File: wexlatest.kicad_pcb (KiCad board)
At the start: 2 copper layers, 51 parts, among them J1 Screw_Terminal_01x02, J2 Conn_02x10_Odd_Even, J3 DB25_Female, J4 PROG, J5 Conn_02x06_Odd_Even, SW1 SW_Push, SW10 SW_DIP_x06, SW2 SW_Push, SW3 SW_Push, SW4 SW_Push, SW5 SW_DIP_x01, SW6 SW_Push, SW7 SW_Push, SW8 SW_Push, SW9 SW_Push

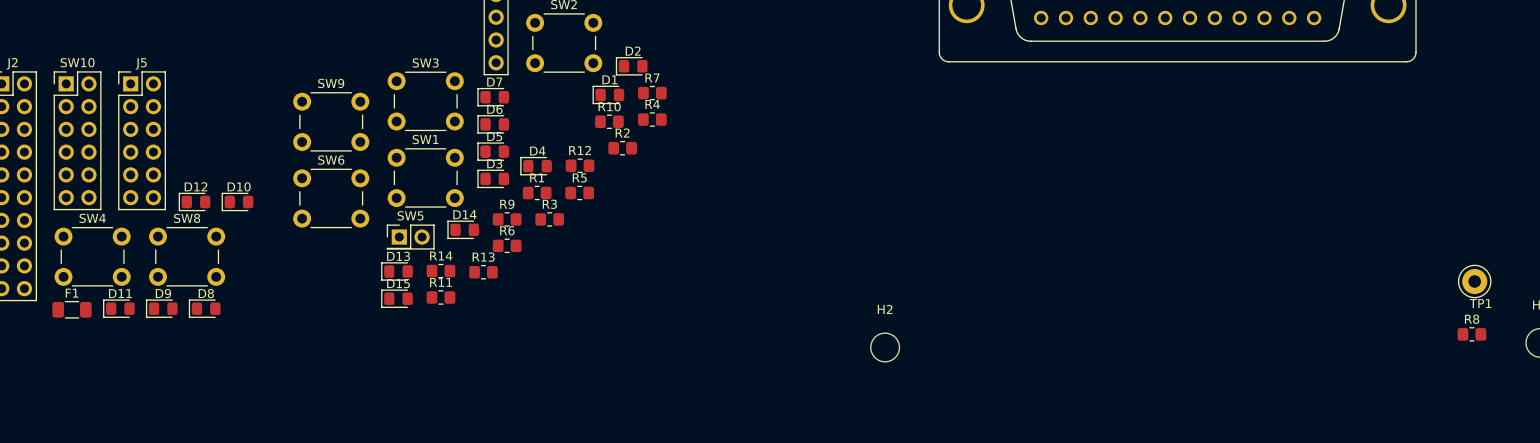
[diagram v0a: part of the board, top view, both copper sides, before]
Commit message: Add KK254 connector.
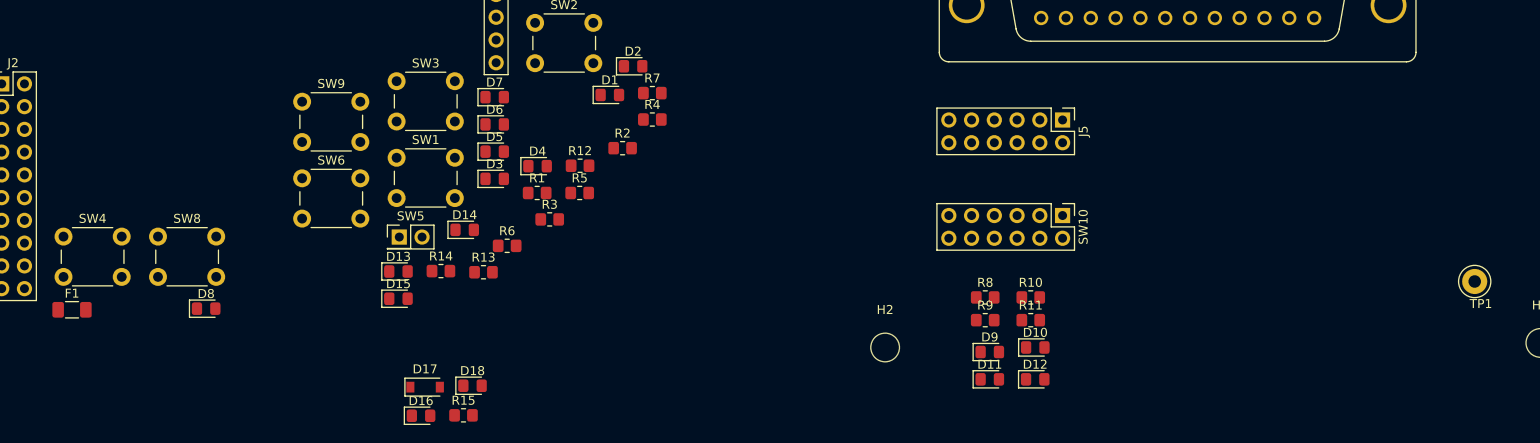
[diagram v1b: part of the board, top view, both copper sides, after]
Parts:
- added D16: GR, LED_SMD:LED_0805_2012Metric_Pad1.15x1.40mm_HandSolder, F.Cu at (73.7, 104.6)
- added D17: 1N4007, Diode_SMD:D_SOD-123, F.Cu at (74.1, 101.5)
- added D18: 1N4148, Diode_SMD:D_0805_2012Metric_Pad1.15x1.40mm_HandSolder, F.Cu at (79.4, 101.3)
- added R15: 1k, Resistor_SMD:R_0805_2012Metric_Pad1.20x1.40mm_HandSolder, F.Cu at (78.4, 104.6)
- moved SW10 112.2 mm to (145.3, 82.3), turned to 270 degrees
- moved J5 104.1 mm to (145.3, 71.6), turned to 270 degrees
- moved D11 97.4 mm to (137.2, 100.6)
- moved D12 95.8 mm to (142.2, 100.6)
- moved D9 92.4 mm to (137.2, 97.5)
- moved D10 90.4 mm to (142.2, 97.0)
- moved R11 65.9 mm to (141.7, 94.0)
- moved R9 54.5 mm to (136.7, 94.0)
- moved R8 54.5 mm to (136.7, 91.4)
- moved R10 51.0 mm to (141.7, 91.4)
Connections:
- D2 pad 1: +12V -> Net-(D17-Pad2)
- D2 pad 2: Net-(D2-Pad2) -> Net-(D18-Pad1)
- F1 pad 2: +12V -> Net-(D17-Pad2)
- R5 pad 1: Net-(D2-Pad2) -> Net-(D18-Pad2)

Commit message: Add initial PCB layout.
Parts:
- added J6: Conn_01x04, Connector_Molex:Molex_KK-254_AE-6410-04A_1x04_P2.54mm_Vertical, F.Cu at (194.1, 76.2)
- R10, R11, R8, R9: moved to B.Cu
- moved F1 185.5 mm to (219.4, 109.2)
- moved J2 156.8 mm to (183.4, 77.2), turned to 270 degrees
- moved D17 151.9 mm to (226.1, 102.1)
- moved D18 140.1 mm to (219.5, 105.7)
- moved SW4 138.0 mm to (169.2, 111.3), turned to 90 degrees
- moved D1 137.4 mm to (227.1, 105.7)
- moved D2 136.4 mm to (226.6, 109.2)
- moved R5 133.4 mm to (223.5, 98.0)
- moved D8 127.9 mm to (171.2, 132.6)
- moved R4 123.1 mm to (218.9, 101.1)
- moved SW5 116.8 mm to (183.9, 115.6), turned to 270 degrees
- moved J4 112.8 mm to (194.8, 54.9)
- moved SW7 112.6 mm to (169.2, 128.5), turned to 90 degrees
- moved SW6 111.6 mm to (160.0, 128.5), turned to 90 degrees
- moved SW9 108.0 mm to (150.9, 128.5), turned to 90 degrees
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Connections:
- SW10 pad 1: Net-(D12-Pad1) -> RELAL
- SW10 pad 10: RELAR -> GND
- SW10 pad 11: RELBL -> RELBR
- SW10 pad 12: RELBR -> Net-(D12-Pad1)
- SW10 pad 2: Net-(D11-Pad1) -> Net-(D9-Pad1)
- SW10 pad 3: Net-(D10-Pad1) -> RELAM
- SW10 pad 4: Net-(D9-Pad1) -> GND
- SW10 pad 5: GND -> RELAR
- SW10 pad 6: GND -> Net-(D10-Pad1)
- SW10 pad 7: RELAM -> RELBL
- SW10 pad 8: RELBM -> Net-(D11-Pad1)
- SW10 pad 9: RELAL -> RELBM

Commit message: PCB: add some wires
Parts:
- moved D2 111.5 mm to (118.1, 83.3), turned to 270 degrees
- moved D1 106.8 mm to (122.7, 83.3), turned to 90 degrees
- moved R5 105.6 mm to (118.1, 92.5), turned to 270 degrees
- moved D18 102.9 mm to (118.1, 87.9), turned to 270 degrees
- moved J1 100.6 mm to (123.0, 103.0), turned to 270 degrees
- moved D17 100.6 mm to (127.3, 83.3), turned to 270 degrees
- moved R4 96.7 mm to (122.7, 92.5), turned to 270 degrees
- moved F1 93.7 mm to (127.3, 92.5), turned to 90 degrees
- moved TP1 92.9 mm to (123.0, 120.0)
- moved J4 47.5 mm to (195.0, 102.4)
- moved H5 37.7 mm to (195.0, 134.0)
- moved H2 37.2 mm to (121.0, 134.0)
- moved D4 34.8 mm to (136.5, 112.4)
- moved R13 33.5 mm to (137.2, 101.0), turned to 0 degrees
- moved D14 33.2 mm to (137.2, 104.8), turned to 0 degrees
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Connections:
- J5 pad 1: RELAL -> RELBL
- J5 pad 10: RELBM -> RELAM
- J5 pad 11: RELBR -> RELAL
- J5 pad 12: RELBR -> RELAL
- J5 pad 2: RELAL -> RELBL
- J5 pad 3: RELAM -> RELBM
- J5 pad 4: RELAM -> RELBM
- J5 pad 5: RELAR -> RELBR
- J5 pad 6: RELAR -> RELBR
- J5 pad 7: RELBL -> RELAR
- J5 pad 8: RELBL -> RELAR
- J5 pad 9: RELBM -> RELAM
- SW10 pad 1: RELAL -> RELBL
- SW10 pad 11: RELBR -> RELAL
- SW10 pad 3: RELAM -> RELBM
- SW10 pad 5: RELAR -> RELBR
- SW10 pad 7: RELBL -> RELAR
- SW10 pad 9: RELBM -> RELAM
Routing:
- net +12V: track 0.00 -> 116.8 mm
- net +5V: track 0.00 -> 75.6 mm, vias 0 -> 2
- net RELAL: track 0.00 -> 66.5 mm
- net RELAM: track 0.00 -> 54.2 mm
- net IN-SLAVE|MCLR: track 0.00 -> 34.8 mm
- net IN-: track 0.00 -> 34.7 mm
- net IN+: track 0.00 -> 34.3 mm
- net RELAR: track 0.00 -> 33.3 mm
- net RELBL: track 0.00 -> 32.5 mm
- net RELBM: track 0.00 -> 31.2 mm
- net RELBR: track 0.00 -> 30.0 mm
- net OUT-: track 0.00 -> 24.8 mm
- net BTN-|PGD: track 0.00 -> 24.7 mm
- net BTN+|PGC: track 0.00 -> 24.7 mm
- net OUT+: track 0.00 -> 24.3 mm
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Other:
- board outline added: 86 x 100 mm
- board text added: "+12V"
- board text added: "+5V"
- board text added: "1"
- board text added: "13"
- board text added: "14"
- board text added: "25"
- board text added: "5V VALID"
- board text added: "BTN+"
- board text added: "BTN-"
- board text added: "GND"
- board text added: "IN+"
- board text added: "IN-"
- board text added: "L"
- board text added: "M"
- board text added: "OUT+"
- board text added: "OUT-"
- board text added: "POWER"
- board text added: "R"
- board text added: "RELA"
- board text added: "RELB"
- board text added: "SHORT"
- board text added: "SLAVE"

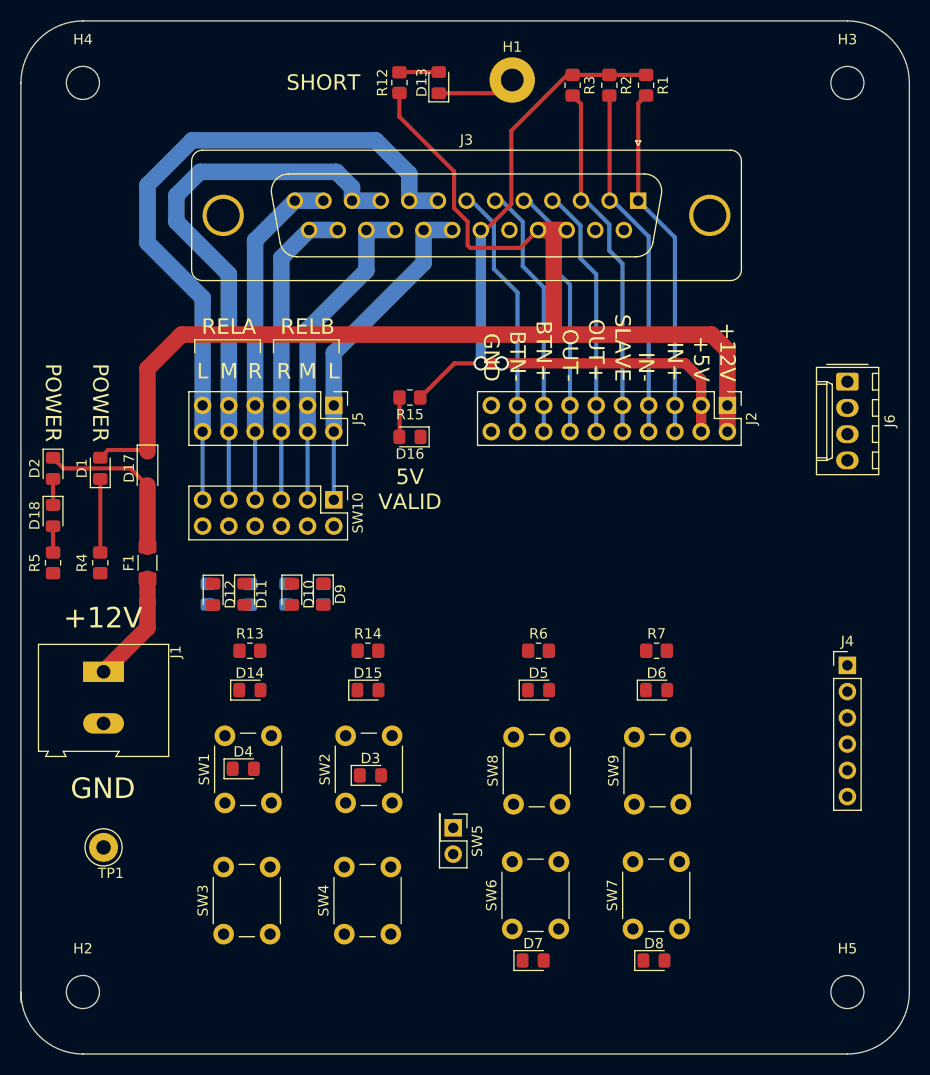
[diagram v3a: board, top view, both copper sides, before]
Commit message: PCB: trace all wires, first prototype.
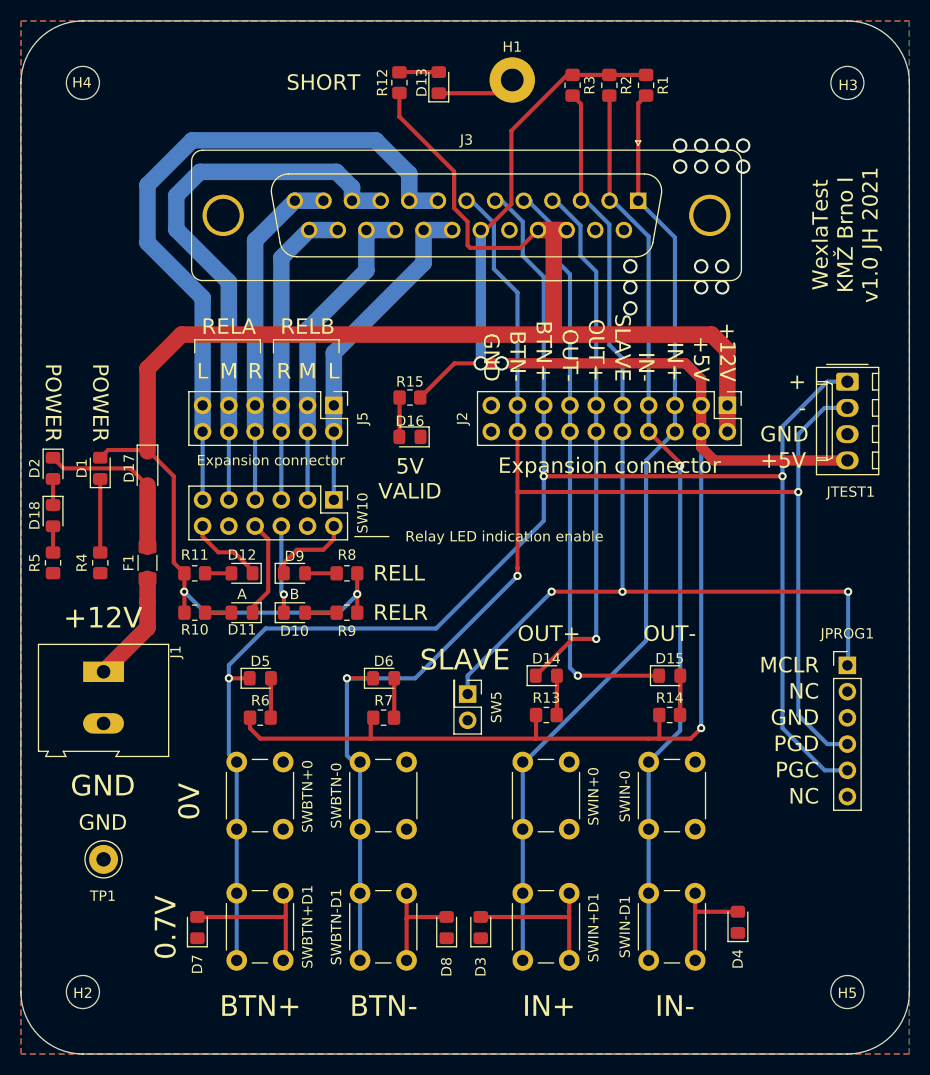
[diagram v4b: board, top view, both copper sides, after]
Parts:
- removed J6: Conn_01x04, Connector_Molex:Molex_KK-254_AE-6410-04A_1x04_P2.54mm_Vertical
- removed SW1, SW2, SW3, SW4, SW8, SW9: SW_Push, Button_Switch_THT:SW_PUSH_6mm
- added JTEST1: Conn_01x04, Connector_Molex:Molex_KK-254_AE-6410-04A_1x04_P2.54mm_Vertical, F.Cu at (195.0, 74.9)
- added SWBTN+0: SW_Push, Button_Switch_THT:SW_PUSH_6mm, F.Cu at (135.9, 118.2)
- added SWBTN-0: SW_Push, Button_Switch_THT:SW_PUSH_6mm, F.Cu at (147.8, 118.2)
- added SWIN+0: SW_Push, Button_Switch_THT:SW_PUSH_6mm, F.Cu at (163.6, 118.2)
- added SWIN+D1: SW_Push, Button_Switch_THT:SW_PUSH_6mm, F.Cu at (163.6, 130.9)
- added SWIN-0: SW_Push, Button_Switch_THT:SW_PUSH_6mm, F.Cu at (175.8, 118.2)
- added SWIN-D1: SW_Push, Button_Switch_THT:SW_PUSH_6mm, F.Cu at (175.8, 130.9)
- R10, R11, R8, R9: moved to F.Cu
- moved D4 50.1 mm to (184.4, 127.3), turned to 90 degrees
- moved D7 32.7 mm to (132.1, 127.8), turned to 90 degrees
- moved R14 29.9 mm to (177.8, 107.2)
- moved R13 29.4 mm to (165.9, 107.2)
- moved D15 29.2 mm to (177.8, 103.4)
- moved D14 28.7 mm to (165.9, 103.4)
- moved R6 27.7 mm to (138.2, 107.4)
- moved R7 27.2 mm to (150.1, 107.4)
- moved D5 26.9 mm to (138.2, 103.6)
- moved SWBTN+D1 26.8 mm to (135.9, 130.9)
- moved SWBTN-D1 26.6 mm to (147.8, 130.9)
- moved D6 26.4 mm to (150.1, 103.6)
- moved D8 20.3 mm to (156.2, 127.8), turned to 90 degrees
- moved D3 18.2 mm to (159.5, 127.8), turned to 90 degrees
- moved SW5 13.0 mm to (158.2, 105.2)
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- renumbered J4 to JPROG1, SW6 to SWBTN+D1, SW7 to SWBTN-D1
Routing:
- net BTN+|PGC: track 24.7 -> 169.8 mm, vias 0 -> 3
- net BTN-|PGD: track 24.7 -> 155.7 mm, vias 0 -> 3
- net +5V: track 75.6 -> 172.7 mm, vias 2 -> 3
- net IN-SLAVE|MCLR: track 34.8 -> 99.4 mm, vias 0 -> 3
- net IN+: track 34.3 -> 92.1 mm
- net IN-: track 34.7 -> 88.4 mm, vias 0 -> 1
- net +12V: track 116.8 -> 156.4 mm, vias 0 -> 2
- net OUT-: track 24.8 -> 56.3 mm, vias 0 -> 1
- net OUT+: track 24.3 -> 51.9 mm, vias 0 -> 1
- net Net-(D3-Pad2): track 0.00 -> 15.2 mm
- net Net-(D7-Pad2): track 0.00 -> 15.1 mm
- net Net-(D4-Pad2): track 0.00 -> 10.7 mm
- net Net-(D8-Pad2): track 0.00 -> 10.5 mm
- net Net-(D11-Pad1): track 0.00 -> 9.54 mm
- net Net-(D10-Pad1): track 0.00 -> 8.48 mm, vias 0 -> 1
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- added copper zone on B.Cu, net GND
- added copper zone on F.Cu, net GND
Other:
- outline, holes or cut-outs redrawn
- board text added: "+"
- board text added: "-"
- board text added: "0.7V"
- board text added: "0V"
- board text added: "A"
- board text added: "B"
- board text added: "Expansion connector"
- board text added: "MCLR"
- board text added: "NC"
- board text added: "PGC"
- board text added: "PGD"
- board text added: "RELL"
- board text added: "RELR"
- board text added: "Relay LED indication enable"
- board text added: "WexlaTest KMŽ Brno I v1.0 JH 2021"

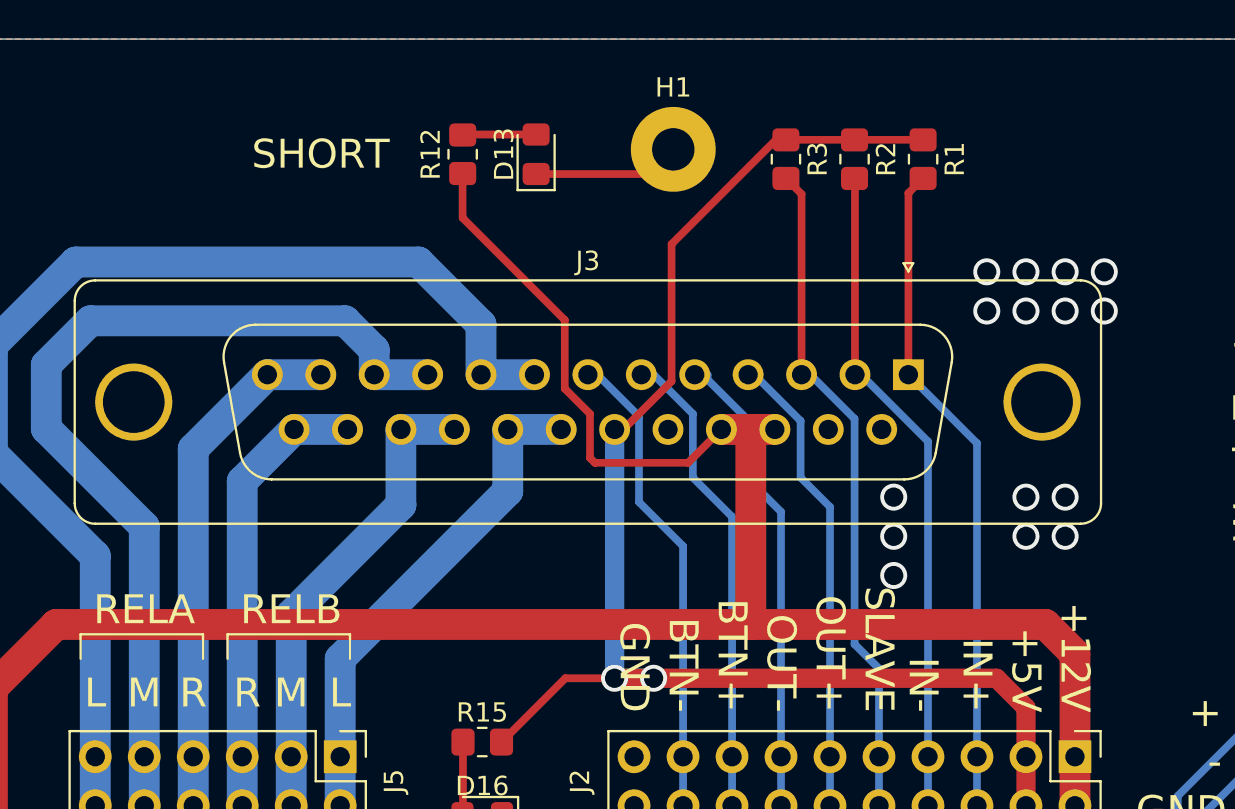
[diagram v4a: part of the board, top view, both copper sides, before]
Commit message: Add holes for mechanical test of turnout force.
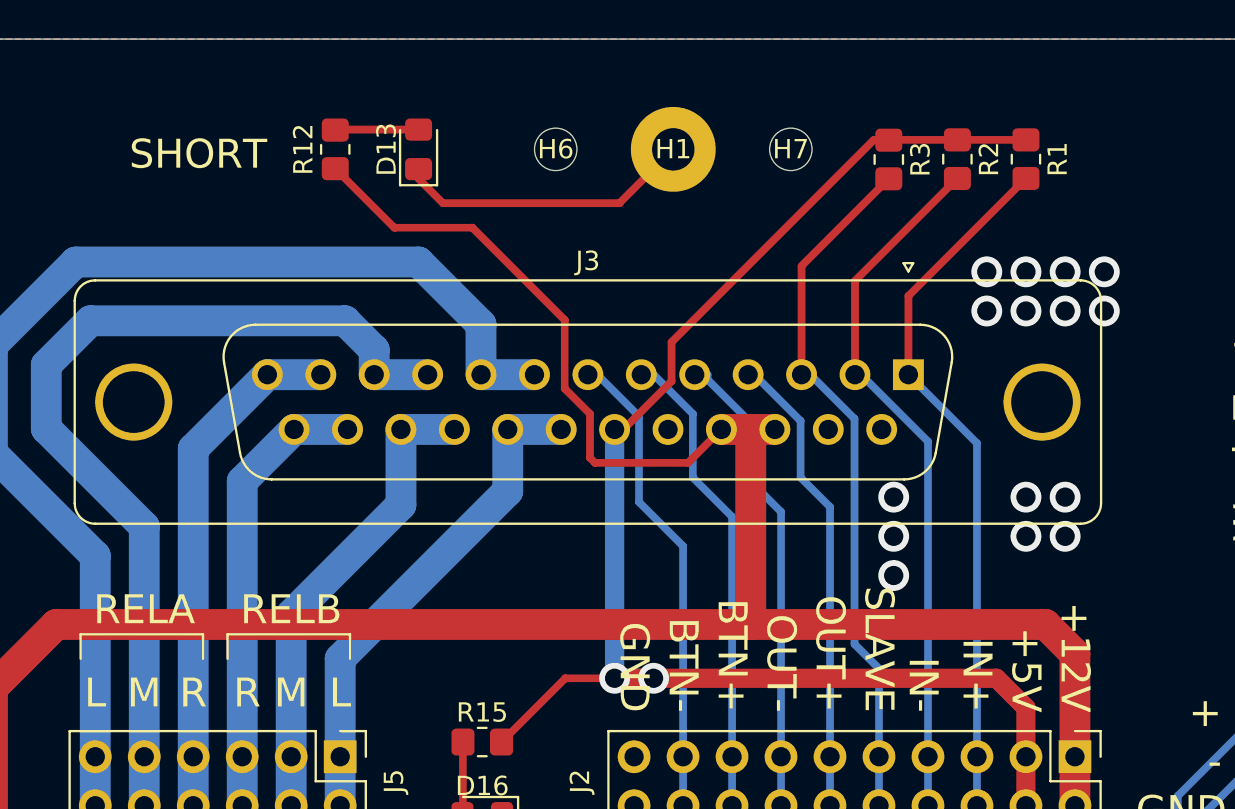
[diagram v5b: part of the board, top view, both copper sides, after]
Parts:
- added H6: MountingHole, MountingHole:MountingHole_2.2mm_M2, F.Cu at (156.5, 45.7)
- added H7: MountingHole, MountingHole:MountingHole_2.2mm_M2, F.Cu at (168.7, 45.7)
- moved R12 6.61 mm to (145.0, 45.7)
- moved D13 6.10 mm to (149.4, 45.7)
- moved R3 5.33 mm to (173.7, 46.2)
- moved R1 5.33 mm to (180.8, 46.2)
- moved R2 5.33 mm to (177.3, 46.2)
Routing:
- net Net-(D13-Pad1): track 7.64 -> 17.4 mm
- net +12V: track 156.4 -> 161.8 mm
- net +5V: track 172.7 -> 175.0 mm
- net IN+: track 92.1 -> 94.3 mm
- net IN-: track 88.4 -> 90.4 mm
- net IN-SLAVE|MCLR: track 99.4 -> 100.9 mm
- net (no net): track 0.00 -> 0.52 mm
- net Net-(D13-Pad2): track 3.82 -> 4.33 mm
